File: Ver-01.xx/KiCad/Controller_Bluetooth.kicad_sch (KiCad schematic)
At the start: 20 parts

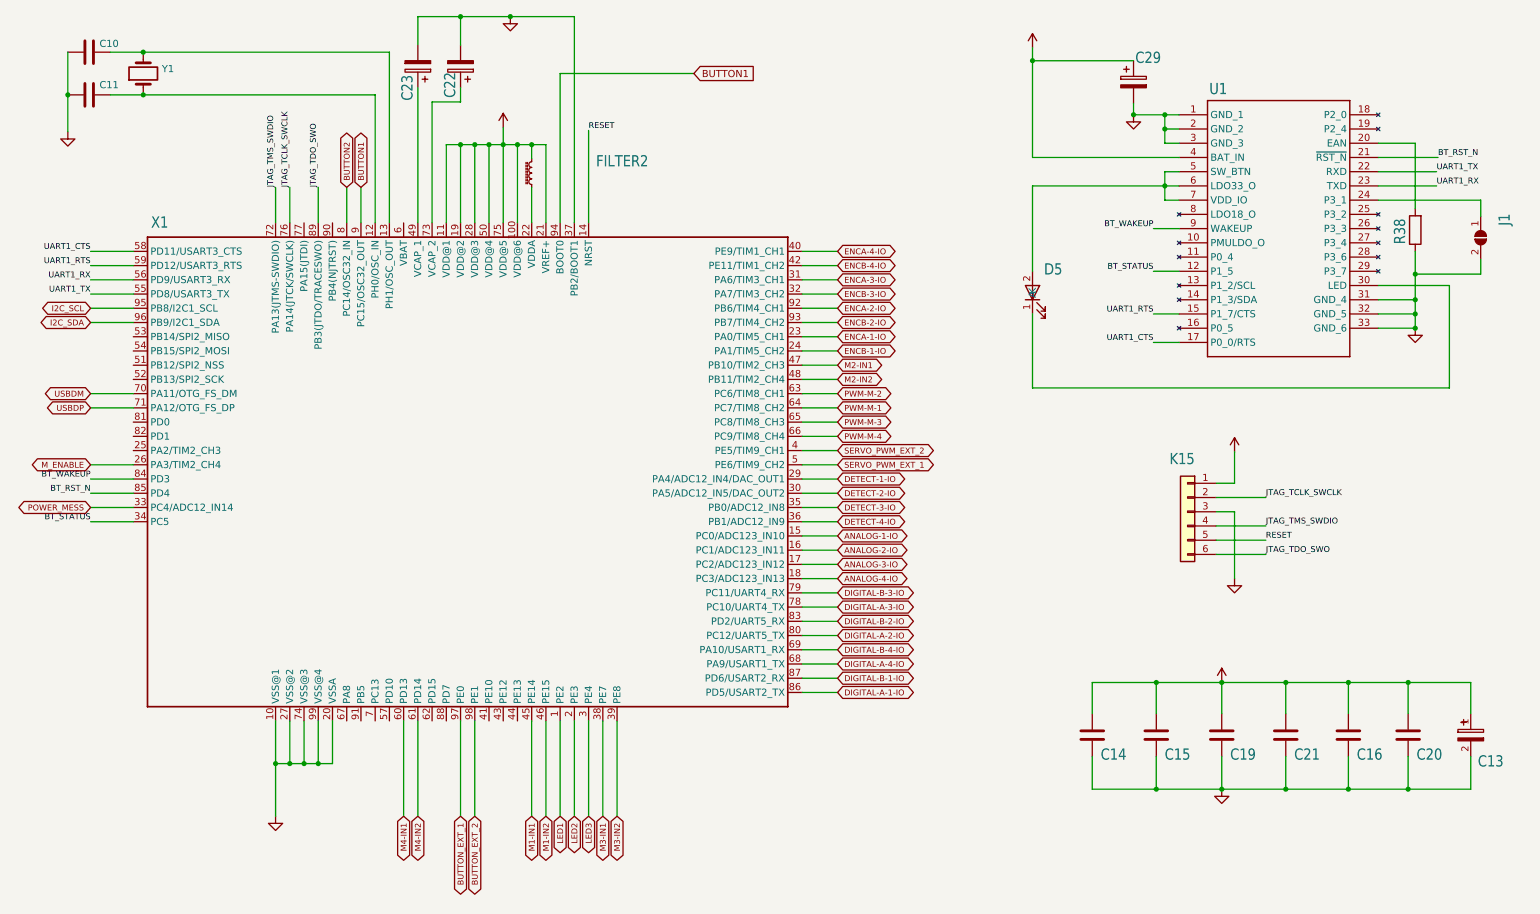
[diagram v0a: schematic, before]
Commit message: Snap to grid
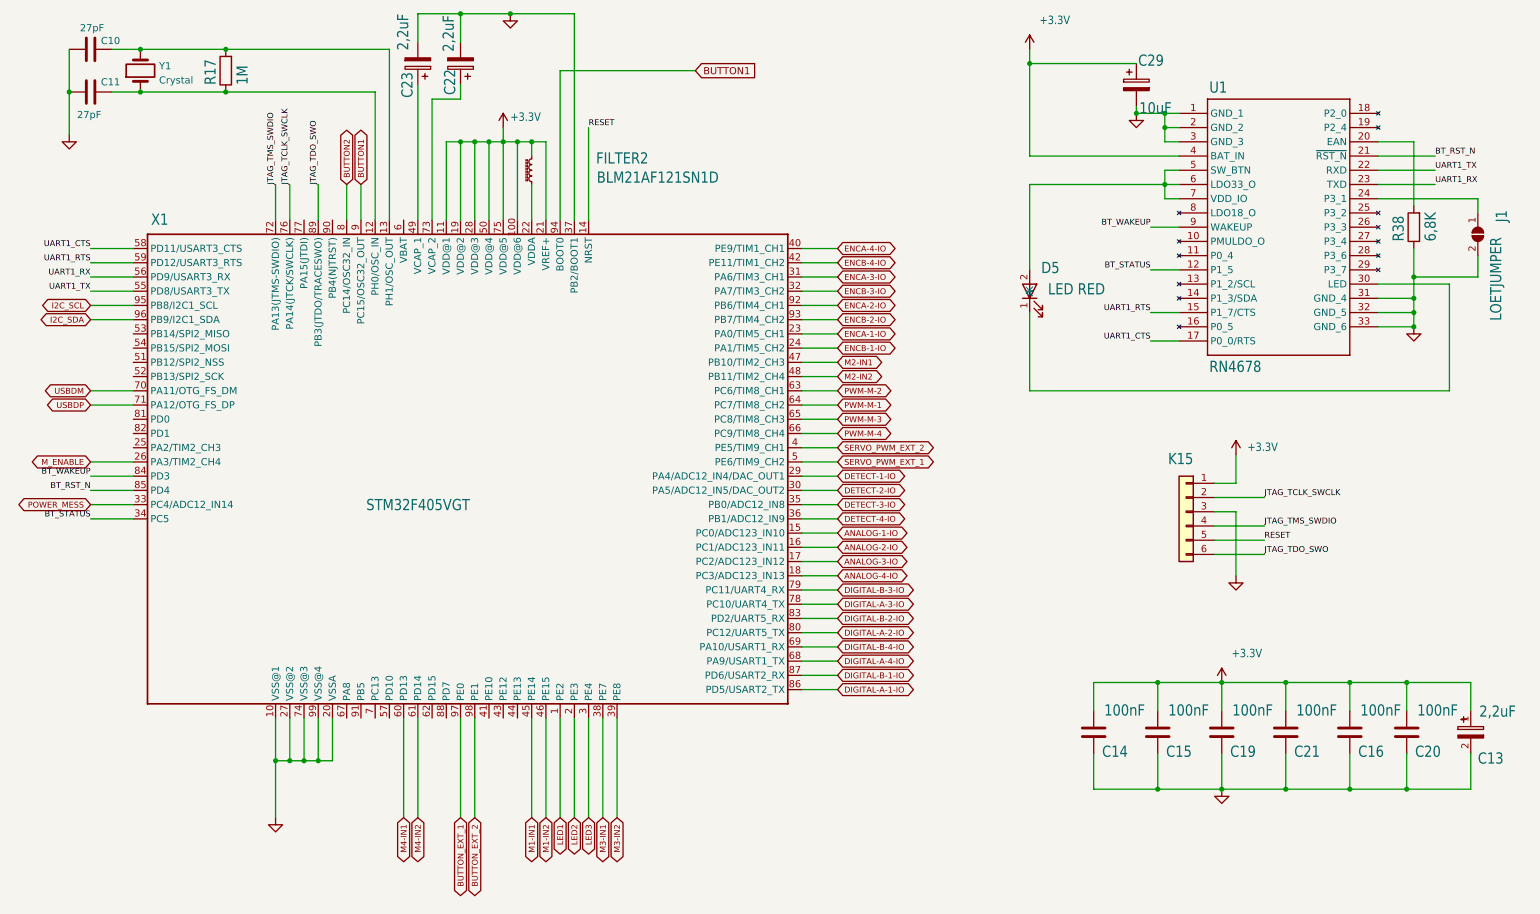
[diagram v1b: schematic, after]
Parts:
- added R17: 1M, Resistor_SMD:R_0603_1608Metric, symbol Device:R
- C10, C11: value (none) -> 27pF; footprint (none) -> Capacitor_SMD:C_0805_2012Metric
- C13, C22, C23: value (none) -> 2,2uF; footprint (none) -> Capacitor_Tantalum_SMD:CP_EIA-3216-10_Kemet-I
- C14, C15, C16, C19, C20, C21: value (none) -> 100nF; footprint (none) -> Capacitor_SMD:C_0805_2012Metric
- C29: value (none) -> 10uF; footprint (none) -> Capacitor_Tantalum_SMD:CP_EIA-3528-12_Kemet-T
- D5: value (none) -> LED RED; footprint (none) -> LED_SMD:LED_0805_2012Metric
- FILTER2: value (none) -> BLM21AF121SN1D; footprint (none) -> Inductor_SMD:L_0805_2012Metric
- J1: value (none) -> LOETJUMPER; footprint (none) -> Jumper:SolderJumper-2_P1.3mm_Open_Pad1.0x1.5mm
- K15: value (none) -> Stiftleiste_1x06; footprint (none) -> Connector_PinHeader_2.54mm:PinHeader_1x06_P2.54mm_Vertical
- R38: value (none) -> 6,8K; footprint (none) -> Resistor_SMD:R_0603_1608Metric
- U1: value (none) -> RN4678; footprint (none) -> ORB:MODULE_RN4678-V_RM100
- X1: value (none) -> STM32F405VGT; footprint (none) -> Package_QFP:LQFP-100_14x14mm_P0.5mm
- Y1: value (none) -> Crystal; footprint (none) -> ORB:XTAL_ECS-80-20-20A-TR
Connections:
- net at C11.2, X1.12 (PH0/OSC_IN), Y1.1: now also R17.1
- net at C10.2, X1.13 (PH1/OSC_OUT), Y1.2: now also R17.2
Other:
- moved on the sheet: C10, C11, C13, C14, C15, C16, C19, C20, C21, C22, C23, C29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

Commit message: Kleinere Optimierungen
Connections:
- net M1-IN1: now also X1.46 (PE15); no longer X1.45 (PE14)
- net M1-IN2: now also X1.45 (PE14); no longer X1.46 (PE15)
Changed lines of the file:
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@@
     (stroke (width 0) (type default) (color 0 0 0 0))
   )
-  (wire (pts (xy 113.03 139.7) (xy 113.03 157.48))
+  (wire (pts (xy 113.03 139.7) (xy 113.03 146.558))
     (stroke (width 0) (type default) (color 0 0 0 0))
   )
@@
     (stroke (width 0) (type default) (color 0 0 0 0))
   )
-  (wire (pts (xy 110.49 157.48) (xy 110.49 139.7))
+  (wire (pts (xy 110.49 146.558) (xy 110.49 139.7))
     (stroke (width 0) (type default) (color 0 0 0 0))
   )
@@
     (stroke (width 0) (type default) (color 0 0 0 0))
   )
-  (wire (pts (xy 80.01 157.48) (xy 80.01 139.7))
+  (wire (pts (xy 102.87 139.7) (xy 102.87 146.558))
+    (stroke (width 0) (type default) (color 0 0 0 0))
+  )
+  (wire (pts (xy 80.01 146.558) (xy 80.01 139.7))
     (stroke (width 0) (type default) (color 0 0 0 0))
   )
@@
     (stroke (width 0) (type default) (color 0 0 0 0))
   )
-  (wire (pts (xy 82.55 157.48) (xy 82.55 139.7))
+  (wire (pts (xy 82.55 146.558) (xy 82.55 139.7))
     (stroke (width 0) (type default) (color 0 0 0 0))
   )
@@
     (stroke (width 0) (type default) (color 0 0 0 0))
   )
-  (wire (pts (xy 105.41 157.48) (xy 105.41 139.7))
-    (stroke (width 0) (type default) (color 0 0 0 0))
-  )
   (wire (pts (xy 260.35 67.31) (xy 254 67.31))
     (stroke (width 0) (type default) (color 0 0 0 0))
@@
     (stroke (width 0) (type default) (color 0 0 0 0))
   )
-  (wire (pts (xy 115.57 157.48) (xy 115.57 139.7))
+  (wire (pts (xy 115.57 146.558) (xy 115.57 139.7))
     (stroke (width 0) (type default) (color 0 0 0 0))
   )
@@
     (stroke (width 0) (type default) (color 0 0 0 0))
   )
-  (wire (pts (xy 118.11 157.48) (xy 118.11 139.7))
+  (wire (pts (xy 118.11 146.558) (xy 118.11 139.7))
     (stroke (width 0) (type default) (color 0 0 0 0))
   )
@@
     (stroke (width 0) (type default) (color 0 0 0 0))
   )
-  (wire (pts (xy 107.95 157.48) (xy 107.95 139.7))
+  (wire (pts (xy 107.95 146.558) (xy 107.95 139.7))
     (stroke (width 0) (type default) (color 0 0 0 0))
   )
@@
     (stroke (width 0) (type default) (color 0 0 0 0))
   )
-  (wire (pts (xy 92.71 157.48) (xy 92.71 139.7))
+  (wire (pts (xy 92.71 146.558) (xy 92.71 139.7))
     (stroke (width 0) (type default) (color 0 0 0 0))
   )
@@
     (stroke (width 0) (type default) (color 0 0 0 0))
   )
+  (wire (pts (xy 105.41 139.7) (xy 105.41 146.558))
+    (stroke (width 0) (type default) (color 0 0 0 0))
+  )
   (wire (pts (xy 151.13 68.58) (xy 157.48 68.58))
     (stroke (width 0) (type default) (color 0 0 0 0))
@@
     (stroke (width 0) (type default) (color 0 0 0 0))
   )
-  (wire (pts (xy 90.17 139.7) (xy 90.17 157.48))
+  (wire (pts (xy 90.17 139.7) (xy 90.17 146.558))
     (stroke (width 0) (type default) (color 0 0 0 0))
   )
@@
     (stroke (width 0) (type default) (color 0 0 0 0))
   )
-  (wire (pts (xy 102.87 157.48) (xy 102.87 139.7))
-    (stroke (width 0) (type default) (color 0 0 0 0))
-  )
   (wire (pts (xy 24.13 99.06) (xy 31.75 99.06))
     (stroke (width 0) (type default) (color 0 0 0 0))
@@
     )
   )
-  (global_label "LED2" (shape bidirectional) (at 110.49 157.48 270) (fields_autoplaced)
-    (effects (font (size 1.05 1.05)) (justify right))
-    (property "Intersheet References" "${INTERSHEET_REFS}" (id 0) (at 110.4244 163.3251 90)
+  (global_label "LED2" (shape bidirectional) (at 110.49 146.558 270) (fields_autoplaced)
+    (effects (font (size 1.05 1.05)) (justify right))
+    (property "Intersheet References" "${INTERSHEET_REFS}" (id 0) (at 110.4244 152.4031 90)
       (effects (font (size 1.05 1.05)) (justify right) hide)
     )
@@
     )
   )
-  (global_label "M3-IN2" (shape bidirectional) (at 118.11 157.48 270) (fields_autoplaced)
-    (effects (font (size 1.05 1.05)) (justify right))
-    (property "Intersheet References" "${INTERSHEET_REFS}" (id 0) (at 176.53 -293.0525 0)
-      (effects (font (size 1.27 1.27)) hide)
-    )
-  )
-  (global_label "LED1" (shape bidirectional) (at 107.95 157.48 270) (fields_autoplaced)
-    (effects (font (size 1.05 1.05)) (justify right))
-    (property "Intersheet References" "${INTERSHEET_REFS}" (id 0) (at 107.8844 163.3251 90)
+  (global_label "M3-IN2" (shape bidirectional) (at 118.11 146.558 270) (fields_autoplaced)
+    (effects (font (size 1.05 1.05)) (justify right))
+    (property "Intersheet References" "${INTERSHEET_REFS}" (id 0) (at 176.53 -303.9745 0)
+      (effects (font (size 1.27 1.27)) hide)
+    )
+  )
+  (global_label "LED1" (shape bidirectional) (at 107.95 146.558 270) (fields_autoplaced)
+    (effects (font (size 1.05 1.05)) (justify right))
+    (property "Intersheet References" "${INTERSHEET_REFS}" (id 0) (at 107.8844 152.4031 90)
       (effects (font (size 1.05 1.05)) (justify right) hide)
     )
   )
-  (global_label "M4-IN2" (shape bidirectional) (at 82.55 157.48 270) (fields_autoplaced)
-    (effects (font (size 1.05 1.05)) (justify right))
-    (property "Intersheet References" "${INTERSHEET_REFS}" (id 0) (at 140.97 -257.4925 0)
+  (global_label "M4-IN2" (shape bidirectional) (at 82.55 146.558 270) (fields_autoplaced)
+    (effects (font (size 1.05 1.05)) (justify right))
+    (property "Intersheet References" "${INTERSHEET_REFS}" (id 0) (at 140.97 -268.4145 0)
       (effects (font (size 1.27 1.27)) hide)
     )
@@
     )
   )
-  (global_label "M3-IN1" (shape bidirectional) (at 115.57 157.48 270) (fields_autoplaced)
-    (effects (font (size 1.05 1.05)) (justify right))
-    (property "Intersheet References" "${INTERSHEET_REFS}" (id 0) (at 173.99 -290.5125 0)
+  (global_label "M3-IN1" (shape bidirectional) (at 115.57 146.558 270) (fields_autoplaced)
+    (effects (font (size 1.05 1.05)) (justify right))
+    (property "Intersheet References" "${INTERSHEET_REFS}" (id 0) (at 173.99 -301.4345 0)
       (effects (font (size 1.27 1.27)) hide)
     )
@@
     )
   )
-  (global_label "M1-IN1" (shape bidirectional) (at 102.87 157.48 270) (fields_autoplaced)
-    (effects (font (size 1.05 1.05)) (justify right))
-    (property "Intersheet References" "${INTERSHEET_REFS}" (id 0) (at 161.29 -277.8125 0)
-      (effects (font (size 1.27 1.27)) hide)
-    )
-  )
-  (global_label "BUTTON_EXT_2" (shape bidirectional) (at 92.71 157.48 270) (fields_autoplaced)
-    (effects (font (size 1.05 1.05)) (justify right))
-    (property "Intersheet References" "${INTERSHEET_REFS}" (id 0) (at 151.13 -267.6525 0)
+  (global_label "M1-IN1" (shape bidirectional) (at 105.41 146.558 270) (fields_autoplaced)
+    (effects (font (size 1.05 1.05)) (justify right))
+    (property "Intersheet References" "${INTERSHEET_REFS}" (id 0) (at 163.83 -288.7345 0)
+      (effects (font (size 1.27 1.27)) hide)
+    )
+  )
+  (global_label "BUTTON_EXT_2" (shape bidirectional) (at 92.71 146.558 270) (fields_autoplaced)
+    (effects (font (size 1.05 1.05)) (justify right))
+    (property "Intersheet References" "${INTERSHEET_REFS}" (id 0) (at 151.13 -278.5745 0)
       (effects (font (size 1.27 1.27)) hide)
     )
@@
     )
   )
-  (global_label "M1-IN2" (shape bidirectional) (at 105.41 157.48 270) (fields_autoplaced)
-    (effects (font (size 1.05 1.05)) (justify right))
-    (property "Intersheet References" "${INTERSHEET_REFS}" (id 0) (at 163.83 -280.3525 0)
+  (global_label "M1-IN2" (shape bidirectional) (at 102.87 146.558 270) (fields_autoplaced)
+    (effects (font (size 1.05 1.05)) (justify right))
+    (property "Intersheet References" "${INTERSHEET_REFS}" (id 0) (at 161.29 -291.2745 0)
       (effects (font (size 1.27 1.27)) hide)
     )
@@
     )
   )
-  (global_label "M4-IN1" (shape bidirectional) (at 80.01 157.48 270) (fields_autoplaced)
-    (effects (font (size 1.05 1.05)) (justify right))
-    (property "Intersheet References" "${INTERSHEET_REFS}" (id 0) (at 138.43 -254.9525 0)
-      (effects (font (size 1.27 1.27)) hide)
-    )
-  )
-  (global_label "LED3" (shape bidirectional) (at 113.03 157.48 270) (fields_autoplaced)
-    (effects (font (size 1.05 1.05)) (justify right))
-    (property "Intersheet References" "${INTERSHEET_REFS}" (id 0) (at 171.45 -287.9725 0)
+  (global_label "M4-IN1" (shape bidirectional) (at 80.01 146.558 270) (fields_autoplaced)
+    (effects (font (size 1.05 1.05)) (justify right))
+    (property "Intersheet References" "${INTERSHEET_REFS}" (id 0) (at 138.43 -265.8745 0)
+      (effects (font (size 1.27 1.27)) hide)
+    )
+  )
+  (global_label "LED3" (shape bidirectional) (at 113.03 146.558 270) (fields_autoplaced)
+    (effects (font (size 1.05 1.05)) (justify right))
+    (property "Intersheet References" "${INTERSHEET_REFS}" (id 0) (at 171.45 -298.8945 0)
       (effects (font (size 1.27 1.27)) hide)
     )
@@
     )
   )
-  (global_label "BUTTON_EXT_1" (shape bidirectional) (at 90.17 157.48 270) (fields_autoplaced)
-    (effects (font (size 1.05 1.05)) (justify right))
-    (property "Intersheet References" "${INTERSHEET_REFS}" (id 0) (at 148.59 -265.1125 0)
-      (effects (font (size 1.27 1.27)) hide)
-    )
+  (global_label "BUTTON_EXT_1" (shape bidirectional) (at 90.17 146.558 270) (fields_autoplaced)
+    (effects (font (size 1.05 1.05)) (justify right))
+    (property "Intersheet References" "${INTERSHEET_REFS}" (id 0) (at 148.59 -276.0345 0)
+      (effects (font (size 1.27 1.27)) hide)
+    )

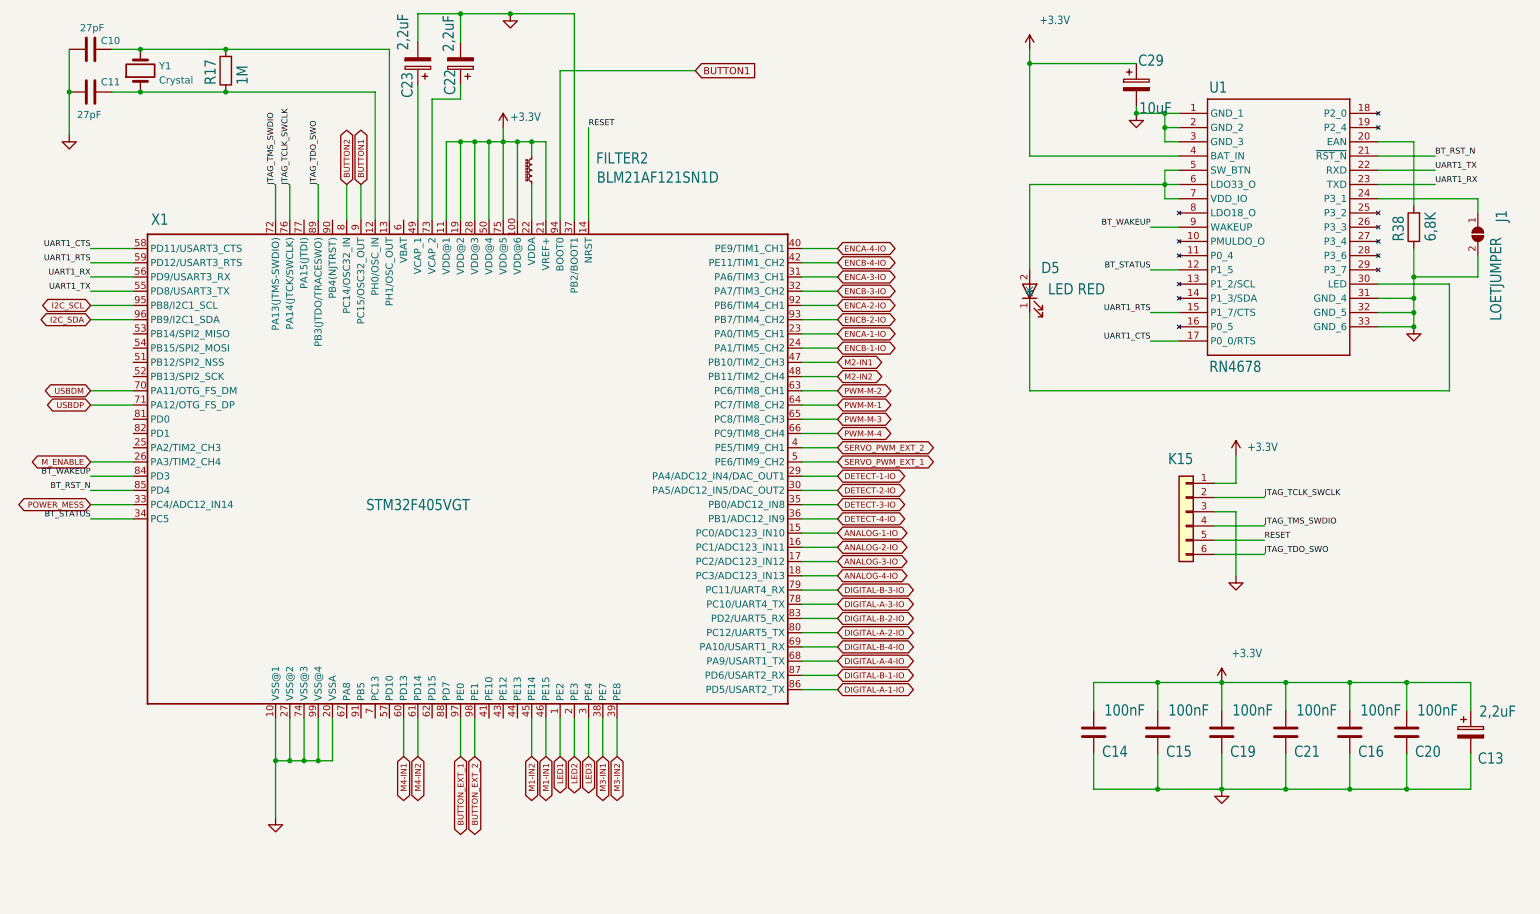
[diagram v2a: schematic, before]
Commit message: R (Crystal) raus, C (Reset) hinzu
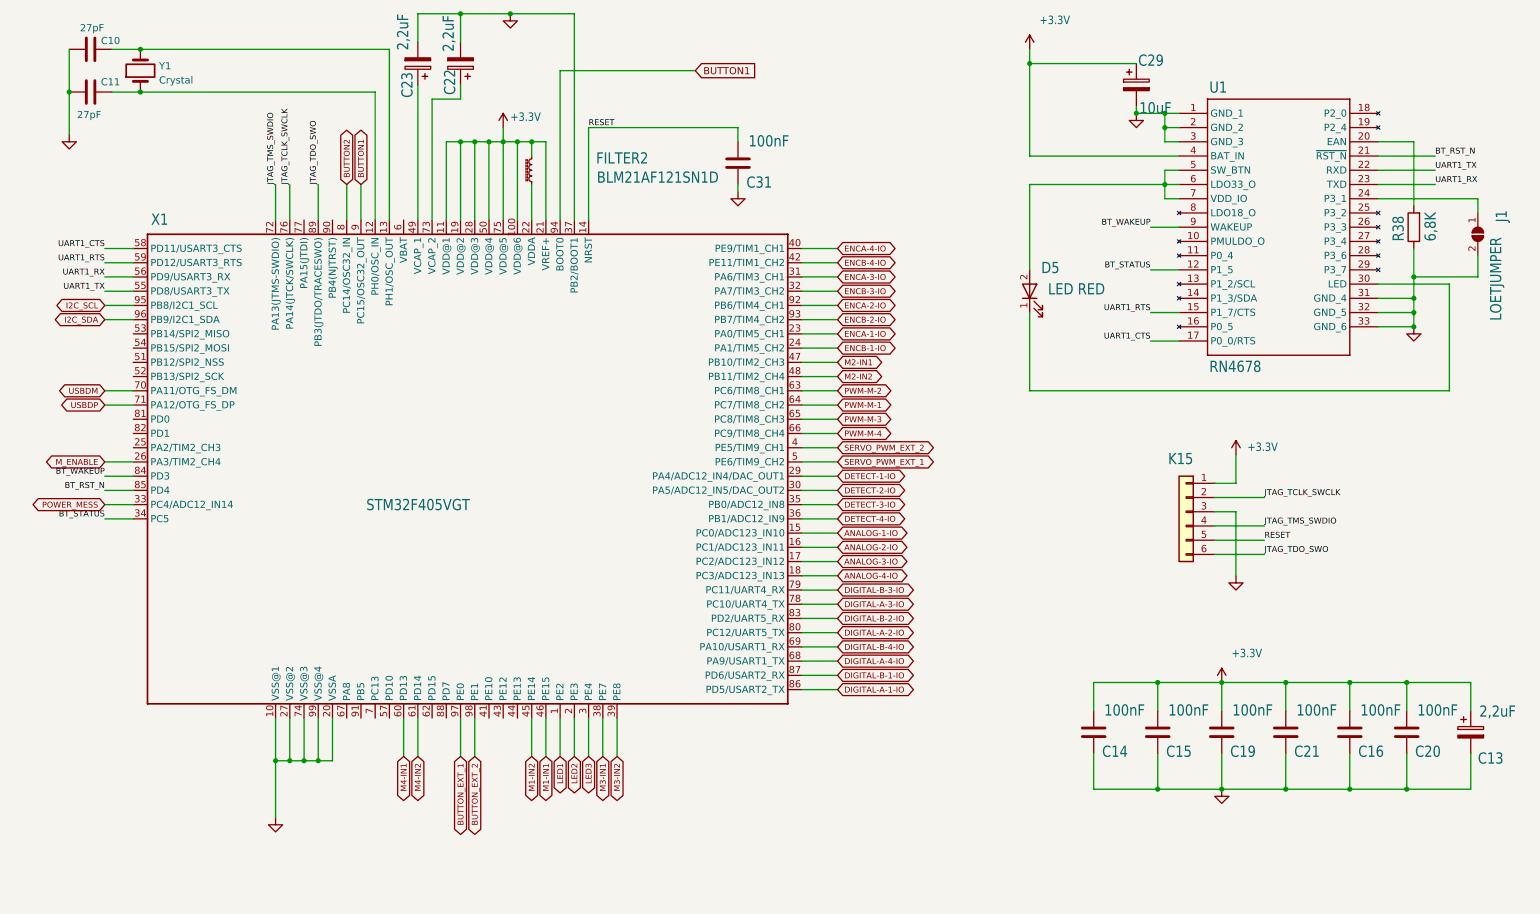
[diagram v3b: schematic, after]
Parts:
- removed R17: 1M, Resistor_SMD:R_0603_1608Metric, symbol Device:R
- added C31: 100nF, Capacitor_SMD:C_0805_2012Metric, symbol Device:C
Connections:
- net GND: now also C31.1
- net RESET: now also C31.2

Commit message: Update KiCad 7.x, Crystal changed
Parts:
- Y1: footprint ORB:XTAL_ECS-80-20-20A-TR -> Crystal:Crystal_SMD_5032-2Pin_5.0x3.2mm; MPN ECS-80-20-20A-TR -> ECS-80-18-30-JGN-TR; OrderNr XC1010TR-ND -> XC2103CT-ND
